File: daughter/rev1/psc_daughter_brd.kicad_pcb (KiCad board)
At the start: 10 copper layers, 40 x 160 mm, 297 parts, among them J1 61082-061400LF, J2 61082-061400LF, U1 AD8221, U10 BUF634AIDR, U11 BUF634AIDR, U12 ADR1001AEZ, U13 ADS8568SPM, U14 AD8221, U15 OPA277, U16 AD8221, U17 OPA277, U18 AD8221, U19 OPA277, U2 OPA277, U20 LT3042xMSE, U27 AD8429BRZ, U28 AD8675ARZ, U3 AD8676ARZ, U30 LTC6363IMS8, U31 LTC2376CDE-20, U32 LTC6655BHLS8-5, U33 AD8429BRZ, U34 AD8675ARZ, U35 LT6202CS5, U36 LTC6363IMS8, U37 LTC2376CDE-20, U38 TXUN0104RUTR, U39 ADUM5240ARZ, U40 ADUM5240ARZ, U41 TXUN0104RUTR, U42 ADUM5242ARZ, U43 ADUM5242ARZ, U5 AD5791BRUZ, U6 AD797ARZ, U7 OPA277, U9 OPA277

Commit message: Change adc driver to ADA4945
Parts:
- removed C134, C169: 6800pF, Capacitor_SMD:C_0402_1005Metric
- removed R50, R62: 10, Resistor_SMD:R_0402_1005Metric
- removed R51, R63: 15, Resistor_SMD:R_0402_1005Metric
- removed U30, U36: LTC6363IMS8, Package_SO:MSOP-8_3x3mm_P0.65mm
- added C109: 4.7nF, Capacitor_SMD:C_0402_1005Metric, F.Cu at (149.9, 70.8)
- added C110: 4.7nF, Capacitor_SMD:C_0402_1005Metric, F.Cu at (158.9, 70.8)
- added C111: 22nF, Capacitor_SMD:C_0402_1005Metric, F.Cu at (146.1, 81.5)
- added C112: 22nF, Capacitor_SMD:C_0402_1005Metric, F.Cu at (154.7, 81.6)
- added C113: 22nF, Capacitor_SMD:C_0402_1005Metric, F.Cu at (151.2, 81.5)
- added C114: 22nF, Capacitor_SMD:C_0402_1005Metric, F.Cu at (160.0, 81.6)
- added R35: 1.0K, Resistor_SMD:R_0402_1005Metric, F.Cu at (149.2, 81.5)
- added R37: 1.0K, Resistor_SMD:R_0402_1005Metric, F.Cu at (157.8, 81.6)
- added R38: 1.0K, Resistor_SMD:R_0402_1005Metric, F.Cu at (148.1, 81.5)
- added R39: 1.0K, Resistor_SMD:R_0402_1005Metric, F.Cu at (156.8, 81.6)
- added R40: 1.0K, Resistor_SMD:R_0402_1005Metric, F.Cu at (150.2, 81.5)
- added R41: 1.0K, Resistor_SMD:R_0402_1005Metric, F.Cu at (158.9, 81.6)
- added R44: 1.0K, Resistor_SMD:R_0402_1005Metric, F.Cu at (147.1, 81.5)
- added R45: 1.0K, Resistor_SMD:R_0402_1005Metric, F.Cu at (155.7, 81.6)
- added R47: 4.64k, Resistor_SMD:R_0402_1005Metric, F.Cu at (147.6, 70.8)
- added R48: 4.64k, Resistor_SMD:R_0402_1005Metric, F.Cu at (156.6, 70.8)
- added U4: ADA4945-1, myparts:QFN50P300X300X80-17N, F.Cu at (148.6, 85.1)
- added U8: ADA4945-1, myparts:QFN50P300X300X80-17N, F.Cu at (157.4, 85.1)
- R46, R58: value 1.3K -> 4.64k
- moved C171 2.50 mm to (145.7, 86.8)
- moved C136 2.45 mm to (154.4, 86.6)
- moved C137 2.14 mm to (160.1, 86.6), turned to 0 degrees
- moved C172 2.06 mm to (151.1, 86.5), turned to 0 degrees
- moved C138 1.51 mm to (154.2, 83.8), turned to 180 degrees
- moved C173 1.35 mm to (145.4, 83.8), turned to 180 degrees
- moved C132 1.34 mm to (159.2, 80.0)
- moved C133 1.34 mm to (157.2, 80.0)
- moved C167 1.27 mm to (150.6, 80.0)
- moved C168 1.27 mm to (148.6, 80.0)
- moved C124 1.06 mm to (156.6, 69.7)
- moved R46 1.06 mm to (158.9, 69.7)
- moved C119 1.04 mm to (154.8, 65.0)
- moved D5 1.04 mm to (157.8, 54.0)
- moved R36 1.04 mm to (157.8, 59.7)
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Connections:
- C124 pad 1: Net-(U28-+) -> Net-(C124-Pad1)
- C124 pad 2: GND -> Net-(U28--)
- C132 pad 2: Net-(C132-Pad2) -> Net-(U28--)
- C133 pad 1: Net-(C132-Pad2) -> Net-(U28--)
- C133 pad 2: Net-(C133-Pad2) -> GND
- C159 pad 1: Net-(U34-+) -> Net-(C159-Pad1)
- C159 pad 2: GND -> Net-(U34--)
- C167 pad 2: Net-(C167-Pad2) -> Net-(U34--)
- C168 pad 1: Net-(C167-Pad2) -> Net-(U34--)
- C168 pad 2: Net-(C168-Pad2) -> GND
- R46 pad 1: Net-(U28-+) -> Net-(C124-Pad1)
- R58 pad 1: Net-(U34-+) -> Net-(C159-Pad1)
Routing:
- net /DCCT ADCs/DCCT Channel 1/drv_vref: track 36.0 -> 5.07 mm, vias 2 -> 0
- net Net-(U34--): track 8.23 -> 17.5 mm, vias 0 -> 2
- net Net-(U28--): track 8.23 -> 17.4 mm, vias 0 -> 2
- net -5.3VA: track 11.5 -> 19.1 mm, vias 4 -> 2
- net +5.3VA: track 14.0 -> 18.5 mm, vias 5 -> 7
- net Net-(C132-Pad2): track 4.31 -> 0.00 mm
- net Net-(C167-Pad2): track 4.31 -> 0.00 mm
- net Net-(C168-Pad2): track 4.30 -> 0.00 mm
- net Net-(C133-Pad2): track 4.30 -> 0.00 mm
- net Net-(C112-Pad1): track 0.00 -> 4.22 mm
- net Net-(C114-Pad1): track 0.00 -> 4.17 mm
- net Net-(C113-Pad1): track 0.00 -> 4.17 mm
- net Net-(C111-Pad1): track 0.00 -> 4.17 mm
- net Net-(U4--FB): track 0.00 -> 3.17 mm
- net Net-(U8-+FB): track 0.00 -> 3.16 mm
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
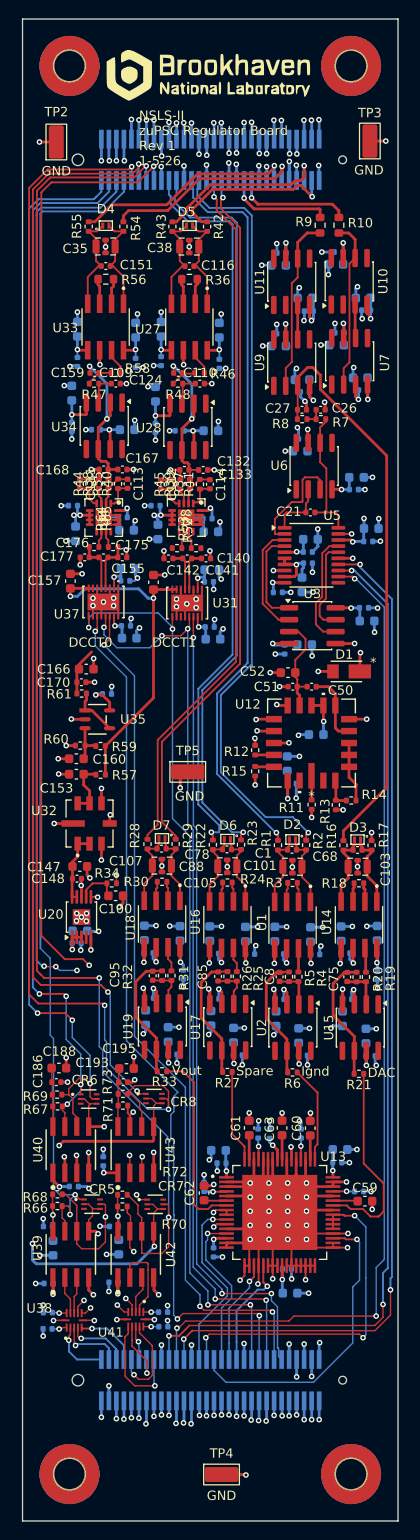
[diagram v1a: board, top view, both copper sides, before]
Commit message: Finish routing of daughterboard
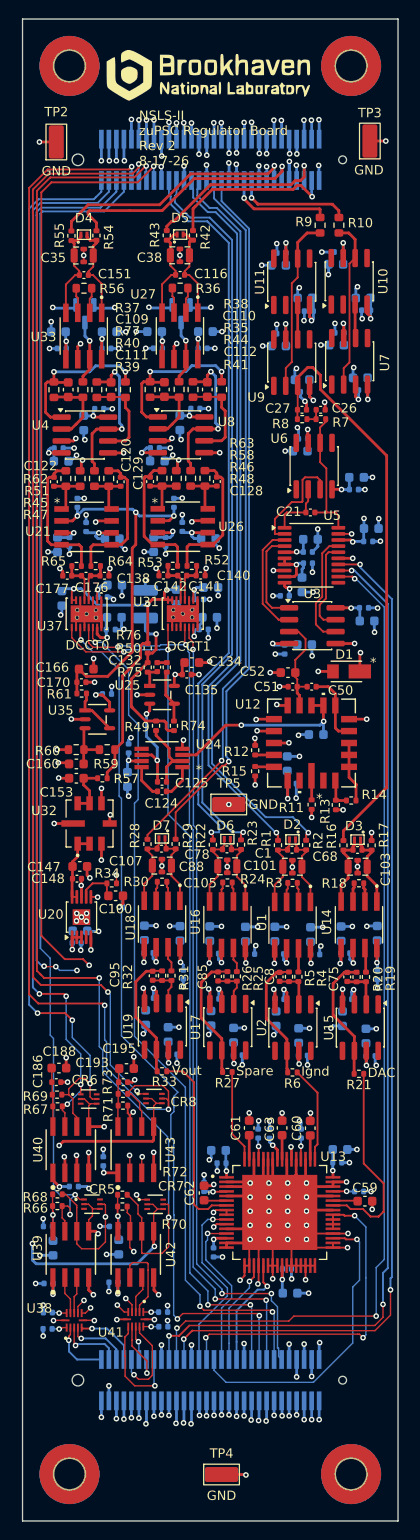
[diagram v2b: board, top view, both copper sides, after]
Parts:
- removed C161: 10uF, Capacitor_SMD:C_0603_1608Metric
- removed C163: 0.1uF, Capacitor_SMD:C_0402_1005Metric
- removed C167, C175: 6800pF, Capacitor_SMD:C_0402_1005Metric
- removed C168: 3300pF, Capacitor_SMD:C_0402_1005Metric
- removed U28, U34: AD8675ARZ, Package_SO:SOIC-8_3.9x4.9mm_P1.27mm
- added C115: 0.1uF, Capacitor_SMD:C_0402_1005Metric, B.Cu at (154.1, 77.7)
- added C118: 10uF, Capacitor_SMD:C_0603_1608Metric, B.Cu at (154.4, 79.1)
- added C120: 470pF, Capacitor_SMD:C_0402_1005Metric, F.Cu at (150.5, 81.3)
- added C122: 470pF, Capacitor_SMD:C_0402_1005Metric, F.Cu at (143.3, 81.3)
- added C125: 4.7uF, Capacitor_SMD:C_0402_1005Metric, F.Cu at (154.9, 113.3)
- added C129: 470pF, Capacitor_SMD:C_0402_1005Metric, F.Cu at (153.6, 81.3)
- added C131: 0.1uF, Capacitor_SMD:C_0402_1005Metric, B.Cu at (151.3, 109.7)
- added C134: 10uF, Capacitor_SMD:C_0603_1608Metric, F.Cu at (158.0, 100.6)
- added C135: 0.1uF, Capacitor_SMD:C_0402_1005Metric, F.Cu at (157.5, 101.8)
- added C149: 0.1uF, Capacitor_SMD:C_0402_1005Metric, B.Cu at (146.8, 86.1)
- added C150: 0.1uF, Capacitor_SMD:C_0402_1005Metric, B.Cu at (156.1, 83.5)
- added D8: BAT54S, Package_TO_SOT_SMD:SOT-23, B.Cu at (146.6, 63.4)
- added D9: BAT54S, Package_TO_SOT_SMD:SOT-23, B.Cu at (156.9, 63.4)
- added R49: 1K, Resistor_SMD:R_0402_1005Metric, F.Cu at (154.2, 107.3)
- added R50: 2, Resistor_SMD:R_0402_1005Metric, F.Cu at (153.3, 101.1)
- added R51: 10.0K, Resistor_SMD:R_0603_1608Metric, F.Cu at (146.1, 80.9)
- added R62: 10.0K, Resistor_SMD:R_0603_1608Metric, F.Cu at (144.6, 80.9)
- added R63: 10.0K, Resistor_SMD:R_0603_1608Metric, F.Cu at (154.9, 80.9)
- added R74: 750, Resistor_SMD:R_0402_1005Metric, F.Cu at (156.1, 107.3)
- added R75: 5.62k, Resistor_SMD:R_0402_1005Metric, F.Cu at (155.4, 101.1)
- added R76: 0, Resistor_SMD:R_0402_1005Metric, F.Cu at (153.3, 99.0)
- added R77: 10.0K, Resistor_SMD:R_0603_1608Metric, F.Cu at (146.4, 71.5)
- added U21: THP210DR, myparts:SOIC_210DR_TEX, F.Cu at (146.8, 86.1)
- added U24: ADA4523-1BRMZ, myparts:RM-8_ADI, F.Cu at (154.9, 110.7)
- added U25: LT6202CS5, myparts:LT6202CS5, F.Cu at (154.9, 104.0)
- added U26: THP210DR, myparts:SOIC_210DR_TEX, F.Cu at (157.1, 86.1)
- C109, C110: value 4.7nF -> 3nF; footprint Capacitor_SMD:C_0402_1005Metric -> Capacitor_SMD:C_0603_1608Metric
- C111, C112: value 22nF -> 2nF; footprint Capacitor_SMD:C_0402_1005Metric -> Capacitor_SMD:C_0603_1608Metric
- C113: value 22nF -> 0.1uF; moved to B.Cu
- C114: value 22nF -> 10uF; footprint Capacitor_SMD:C_0402_1005Metric -> Capacitor_SMD:C_0603_1608Metric; moved to B.Cu
- C124: value 0.01uF -> 0.1uF
- C128: value 0.1uF -> 470pF; moved to F.Cu
- C132: value 6800pF -> 47nF
- C133: value 3300pF -> 47uF; footprint Capacitor_SMD:C_0402_1005Metric -> Capacitor_SMD:C_1210_3225Metric; moved to B.Cu
- C137: value 10uF -> 0.1uF; footprint Capacitor_SMD:C_0603_1608Metric -> Capacitor_SMD:C_0402_1005Metric
- C138: value 0.1uF -> 6800pF; moved to F.Cu
- C139: value 0.1uF -> 10uF; footprint Capacitor_SMD:C_0402_1005Metric -> Capacitor_SMD:C_0603_1608Metric
- C155, C157: moved to B.Cu
- C159: value 0.01uF -> 0.1uF; moved to B.Cu
- R35, R37, R38, R39, R40, R41, R44, R45: value 1.0K -> 10.0K; footprint Resistor_SMD:R_0402_1005Metric -> Resistor_SMD:R_0603_1608Metric
- R46, R47, R48, R58: value 4.64k -> 10.0K; footprint Resistor_SMD:R_0402_1005Metric -> Resistor_SMD:R_0603_1608Metric
- R59, R60: value 10K -> 10.0K; footprint Resistor_SMD:R_0402_1005Metric -> Resistor_SMD:R_0603_1608Metric
- U4, U8: value ADA4945-1 -> AD8676xR; footprint myparts:QFN50P300X300X80-17N -> Package_SO:SOIC-8_3.9x4.9mm_P1.27mm
- moved C124 44.6 mm to (154.9, 114.3)
- moved C126 41.2 mm to (151.2, 113.0), turned to -90 degrees
- moved C132 21.6 mm to (154.4, 101.0), turned to -90 degrees
- moved R37 17.6 mm to (143.3, 71.5), turned to -90 degrees
- moved C173 16.6 mm to (158.4, 73.5), turned to 0 degrees
- moved C171 16.2 mm to (156.8, 75.0)
- moved C114 16.0 mm to (144.1, 79.1), turned to 0 degrees
- moved C137 15.1 mm to (145.0, 87.7), turned to -90 degrees
- moved R44 14.9 mm to (158.2, 71.5), turned to -90 degrees
- moved C133 14.9 mm to (153.1, 94.3), turned to -90 degrees
- moved C159 14.0 mm to (145.8, 83.5), turned to 90 degrees
- moved C127 13.6 mm to (154.0, 88.0), turned to -90 degrees
- moved R58 13.0 mm to (156.4, 80.9), turned to 90 degrees
- moved R35 12.6 mm to (156.7, 71.5)
- moved C130 11.9 mm to (155.2, 87.7), turned to -90 degrees
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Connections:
- net /DCCT ADCs/DCCT Channel 1/adc_vref renamed /DAC/adc_ref_out
- C109 pad 1: Net-(U34-+) -> Net-(U4A--)
- C109 pad 2: GND -> Net-(C109-Pad2)
- C110 pad 1: Net-(U28-+) -> Net-(U8A--)
- C110 pad 2: GND -> Net-(C110-Pad2)
- C111 pad 1: Net-(C111-Pad1) -> Net-(U4B--)
- C111 pad 2: Net-(U4-+FB) -> Net-(C111-Pad2)
- C112 pad 1: Net-(C112-Pad1) -> Net-(U8B--)
- C112 pad 2: Net-(U8-+FB) -> Net-(C112-Pad2)
- C113 pad 1: Net-(C113-Pad1) -> -5.3VA
- C113 pad 2: Net-(U4--FB) -> GND
- C114 pad 1: Net-(C114-Pad1) -> -5.3VA
- C114 pad 2: Net-(U8--FB) -> GND
- C124 pad 1: Net-(C124-Pad1) -> Net-(U24-*SD)
- C124 pad 2: Net-(U28--) -> Net-(U24-SDC)
- C126 pad 1: -15V -> +15V
- C127 pad 1: +15V -> +5.3VA
- C128 pad 1: -15V -> Net-(U26-IN+)
- C128 pad 2: GND -> Net-(U26-OUT-)
- C130 pad 1: +15V -> +5.3VA
- C132 pad 1: GND -> Net-(C132-Pad1)
- C132 pad 2: Net-(U28--) -> Net-(C132-Pad2)
- C133 pad 1: Net-(U28--) -> GND
- C133 pad 2: GND -> Net-(C133-Pad2)
- C137 pad 1: -5.3VA -> +5.3VA
- C138 pad 1: +5.3VA -> GND
- C138 pad 2: GND -> Net-(U37-IN+)
- C159 pad 1: Net-(C159-Pad1) -> /DCCT ADCs/DCCT Channel 1/drv_vref
- C159 pad 2: Net-(U34--) -> GND
- C162 pad 1: +15V -> +5.3VA
- C165 pad 1: +15V -> +5.3VA
- C189 pad 1: +1V8 -> +1.8V
- C29 pad 1: +1.8V -> +3.3V
- R35 pad 1: Net-(C113-Pad1) -> Net-(U8A--)
- R35 pad 2: Net-(U34--) -> Net-(D9-COM)
- R37 pad 1: Net-(C114-Pad1) -> Net-(C109-Pad2)
- R37 pad 2: Net-(U28--) -> Net-(U4A--)
- R38 pad 1: Net-(C111-Pad1) -> Net-(C110-Pad2)
- R38 pad 2: GND -> Net-(U8A--)
- R39 pad 1: Net-(C112-Pad1) -> Net-(U4B--)
- R39 pad 2: GND -> Net-(C109-Pad2)
- R40 pad 1: Net-(U4--FB) -> Net-(C111-Pad2)
- R40 pad 2: Net-(C113-Pad1) -> Net-(U4B--)
- R41 pad 1: Net-(U8--FB) -> Net-(U8B--)
- R41 pad 2: Net-(C114-Pad1) -> Net-(C110-Pad2)
- R44 pad 1: Net-(U4-+FB) -> Net-(C112-Pad2)
- R44 pad 2: Net-(C111-Pad1) -> Net-(U8B--)
- R45 pad 1: Net-(U8-+FB) -> Net-(U21-IN+)
- R45 pad 2: Net-(C112-Pad1) -> Net-(C111-Pad2)
- R46 pad 1: Net-(C124-Pad1) -> Net-(U26-IN+)
- R46 pad 2: Net-(R46-Pad2) -> Net-(C112-Pad2)
- R47 pad 1: Net-(U34-+) -> Net-(U21-OUT-)
- R47 pad 2: Net-(C159-Pad1) -> Net-(U21-IN+)
- R48 pad 1: Net-(U28-+) -> Net-(U26-OUT-)
- R48 pad 2: Net-(C124-Pad1) -> Net-(U26-IN+)
- R52 pad 2: Net-(R52-Pad2) -> Net-(U26-OUT-)
- R53 pad 2: Net-(R53-Pad2) -> Net-(U26-OUT+)
- R58 pad 1: Net-(C159-Pad1) -> Net-(U26-IN-)
- R58 pad 2: Net-(R58-Pad2) -> GND
- R60 pad 1: Net-(U35-+) -> GND
- R60 pad 2: GND -> Net-(U35-+)
- R64 pad 2: Net-(R64-Pad2) -> Net-(U21-OUT-)
- R65 pad 2: Net-(R65-Pad2) -> Net-(U21-OUT+)
- U27 pad 7: Net-(R46-Pad2) -> Net-(D9-COM)
- U33 pad 7: Net-(R58-Pad2) -> Net-(D8-COM)
- U4 pad 1: Net-(U4--FB) -> Net-(C109-Pad2)
- U4 pad 2: Net-(C113-Pad1) -> Net-(U4A--)
- U4 pad 3: Net-(C111-Pad1) -> GND
- U4 pad 4: Net-(U4-+FB) -> -5.3VA
- U4 pad 5: +5.3VA -> GND
- U4 pad 6: +5.3VA -> Net-(U4B--)
- U4 pad 7: +5.3VA -> Net-(C111-Pad2)
- U41 pad 11: +1V8 -> +1.8V
- U5 pad 10: +1.8V -> +3.3V
- U8 pad 1: Net-(U8--FB) -> Net-(C110-Pad2)
- U8 pad 2: Net-(C114-Pad1) -> Net-(U8A--)
- U8 pad 3: Net-(C112-Pad1) -> GND
- U8 pad 4: Net-(U8-+FB) -> -5.3VA
- U8 pad 5: +5.3VA -> GND
- U8 pad 6: +5.3VA -> Net-(U8B--)
- U8 pad 7: +5.3VA -> Net-(C112-Pad2)
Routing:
- net /DCCT ADCs/DCCT Channel 1/drv_vref: track 5.07 -> 40.4 mm, vias 0 -> 3
- net Net-(C133-Pad2): track 0.00 -> 17.9 mm, vias 0 -> 1
- net Net-(C110-Pad2): track 0.00 -> 17.8 mm, vias 0 -> 2
- net Net-(C109-Pad2): track 0.00 -> 17.8 mm, vias 0 -> 2
- net Net-(U34--): track 17.5 -> 0.00 mm, vias 2 -> 0
- net Net-(U28--): track 17.4 -> 0.00 mm, vias 2 -> 0
- net Net-(C111-Pad2): track 0.00 -> 16.7 mm, vias 0 -> 2
- net Net-(C112-Pad2): track 0.00 -> 16.7 mm, vias 0 -> 2
- net Net-(U12-BUF_INP): track 4.39 -> 20.9 mm, vias 1 -> 2
- net Net-(U21-OUT+): track 0.00 -> 15.6 mm
- net GND: track 428.7 -> 444.1 mm, vias 288 -> 286
- net Net-(U26-OUT-): track 0.00 -> 14.9 mm
- net Net-(U26-OUT+): track 0.00 -> 14.7 mm
- net Net-(U21-OUT-): track 0.00 -> 14.7 mm
- net Net-(U25-+): track 0.00 -> 10.7 mm, vias 0 -> 2
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- added copper zone on In7.Cu, net -5.3VA
- removed copper zone on In2.Cu, net -5.3VA
- removed copper zone on In7.Cu, net /DCCT ADCs/dcct_busy
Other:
- board text added: "NSLS-II zuPSC Regulator Board Rev 2 8-17-26"
- board text removed: "NSLS-II zuPSC Regulator Board Rev 1 1-5-26"
